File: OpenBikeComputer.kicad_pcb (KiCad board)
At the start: 4 copper layers, 80 x 80 mm, 46 parts, among them J1 USB_C_Receptacle_USB2.0_14P, J2 RJ45_Shielded, J3 RJ45_Shielded, J4 Micro_SD_Card_Det1, J5 Conn_01x24_Socket, J6 Conn_01x03_Pin, U1 nRF54L15-QFXX, U2 nPM1300-QEXX, U3 BQ298012RUGR, U4 BH-18650-A1BJ021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

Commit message: improve design a lot
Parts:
- removed J3: RJ45_Shielded, Connector_RJ:RJ45_Amphenol_54602-x08_Horizontal
- removed REF**: Wuerth_36103205_20x20mm, RF_Shielding:Wuerth_36103205_20x20mm
- removed REF** (x2): 18650, Library:18650
- removed TH1: Thermistor_NTC, Resistor_SMD:R_2512_6332Metric_Pad1.40x3.35mm_HandSolder
- removed U4: BH-18650-A1BJ021, Library:BAT-TH_L77.0-W39.9_BH-18650-A1BJ021
- added C19: 1.5pF, Capacitor_SMD:C_0201_0603Metric, F.Cu at (204.2, 113.4)
- added C20: 2.0pF, Capacitor_SMD:C_0201_0603Metric, F.Cu at (206.2, 113.1)
- added C21: 0.3pF, Capacitor_SMD:C_0201_0603Metric, F.Cu at (207.3, 115.4)
- added J7: RFShield_TwoPieces, RF_Shielding:Laird_Technologies_BMI-S-103_26.21x26.21mm, F.Cu at (197.5, 112.6)
- added J8: Conn_01x02_Socket, Connector_JST:JST_PH_S2B-PH-K_1x02_P2.00mm_Horizontal, B.Cu at (223.2, 93.1)
- added L3: 2.7nH, Inductor_SMD:L_0201_0603Metric, F.Cu at (204.2, 114.1)
- added L4: 3.5nH, Inductor_SMD:L_0201_0603Metric, F.Cu at (205.9, 114.1)
- added L5: 3.5nH, Inductor_SMD:L_0201_0603Metric, F.Cu at (206.2, 115.1)
- J2: footprint Connector_RJ:RJ45_Amphenol_54602-x08_Horizontal -> Connector_RJ:RJ45_Amphenol_RJHSE538X; moved to B.Cu
- moved U7 75.0 mm to (223.1, 152.5)
- moved U6 75.0 mm to (227.4, 152.3)
- moved C1 60.8 mm to (160.3, 112.9)
- moved C2 60.8 mm to (160.3, 114.9)
- moved C4 60.8 mm to (160.3, 118.8)
- moved R2 60.8 mm to (168.9, 114.9)
- moved R1 60.8 mm to (168.9, 112.9)
- moved C10 60.8 mm to (163.2, 120.8)
- moved C11 60.8 mm to (166.1, 112.9)
- moved C12 60.8 mm to (166.1, 114.9)
- moved C13 60.8 mm to (166.1, 116.8)
- moved C14 60.8 mm to (166.1, 118.8)
- moved C8 60.8 mm to (163.2, 116.8)
- moved C9 60.8 mm to (163.2, 118.8)
- moved U3 29.6 mm to (218.8, 94.8), turned to 180 degrees
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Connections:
- J2 pad 1: unconnected-(J2-Pad1) -> GND
- J2 pad 2: GND -> VDDIO
- J2 pad 3: VDDIO -> DETECT1
- J2 pad 4: SENSE1B -> DETECT2
- J2 pad 6: DETECT1 -> SENSE1B
- J2 pad 7: GND -> SENSE2A
- J2 pad 8: unconnected-(J2-Pad8) -> SENSE2B
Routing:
- net /Battery/NTC: track 32.3 -> 1.31 mm
- net Net-(AE2-A): track 0.00 -> 13.5 mm
- net BATGND: track 0.00 -> 4.22 mm
- net GND: track 4.33 -> 6.79 mm, vias 14 -> 16
- net Net-(C19-Pad1): track 0.00 -> 1.74 mm
- net Net-(C20-Pad1): track 0.00 -> 1.46 mm
- net Net-(U1-ANT): track 0.00 -> 1.09 mm

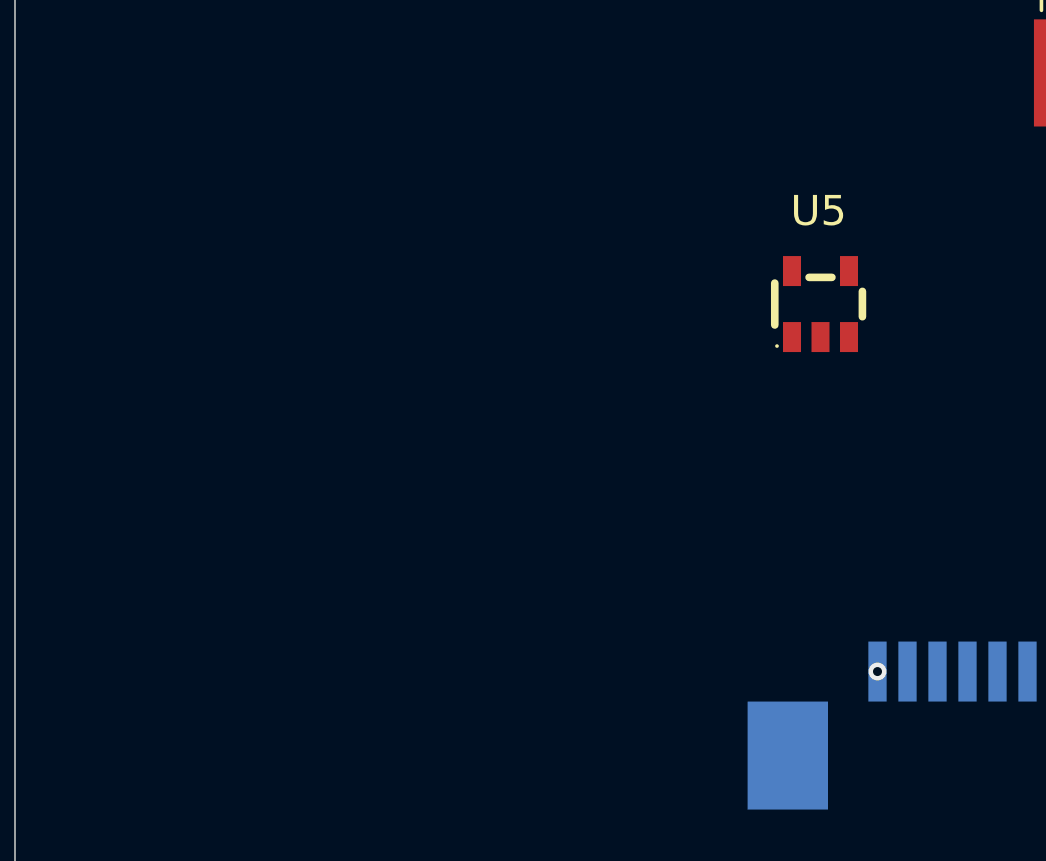
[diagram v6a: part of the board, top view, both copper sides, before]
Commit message: finish oled driver circuit
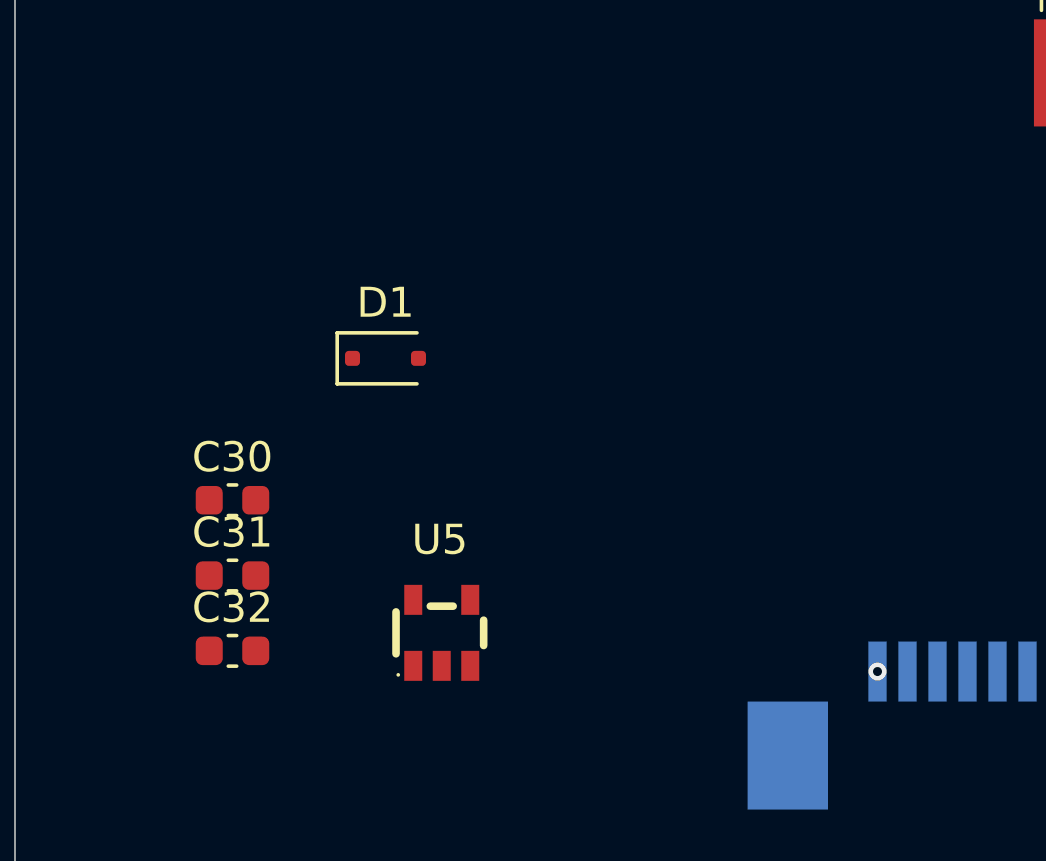
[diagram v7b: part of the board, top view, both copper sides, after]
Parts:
- added C30: 4.7uF, Capacitor_SMD:C_0603_1608Metric, F.Cu at (157.2, 138.5)
- added C31: 120pF, Capacitor_SMD:C_0603_1608Metric, F.Cu at (157.2, 141.1)
- added C32: 4.7uF, Capacitor_SMD:C_0603_1608Metric, F.Cu at (157.2, 143.6)
- added D1: BAT54J, Diode_SMD:D_SOD-323F, F.Cu at (162.3, 133.8)
- moved U5 16.7 mm to (164.2, 143.0)
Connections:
- J5 pad 23: unconnected-(J5-Pin_23-Pad23) -> VOUT
- U1 pad 20: unconnected-(U1-P2.09-Pad20) -> /Display/DISPLAY_SHDN
- U5 pad 1: unconnected-(U5-SW-Pad1) -> Net-(D1-A)
- U5 pad 2: unconnected-(U5-GND-Pad2) -> GND
- U5 pad 3: unconnected-(U5-FB-Pad3) -> Net-(U5-FB)
- U5 pad 4: unconnected-(U5-SHDN#-Pad4) -> /Display/DISPLAY_SHDN
- U5 pad 5: unconnected-(U5-VIN-Pad5) -> /Display/3.0V

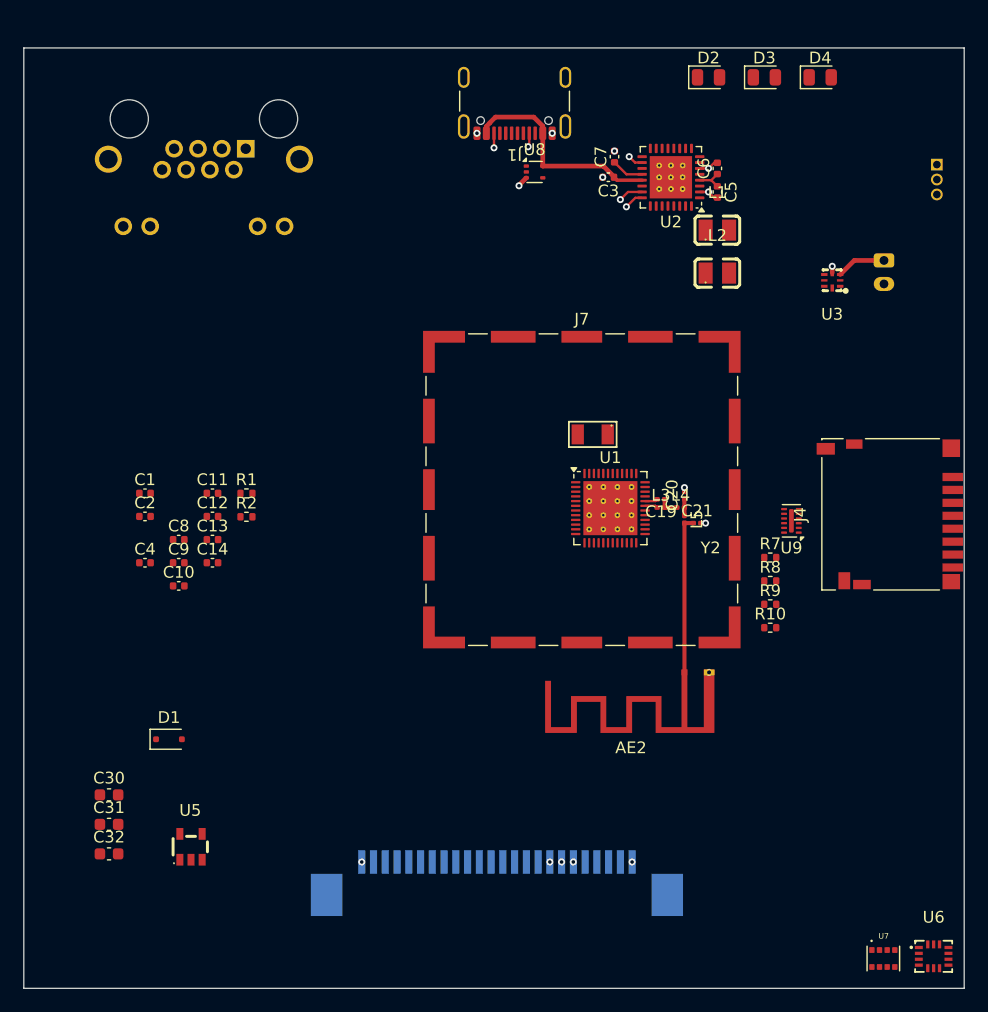
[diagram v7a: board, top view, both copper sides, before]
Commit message: route SD card traces and antenna traces semi-properly
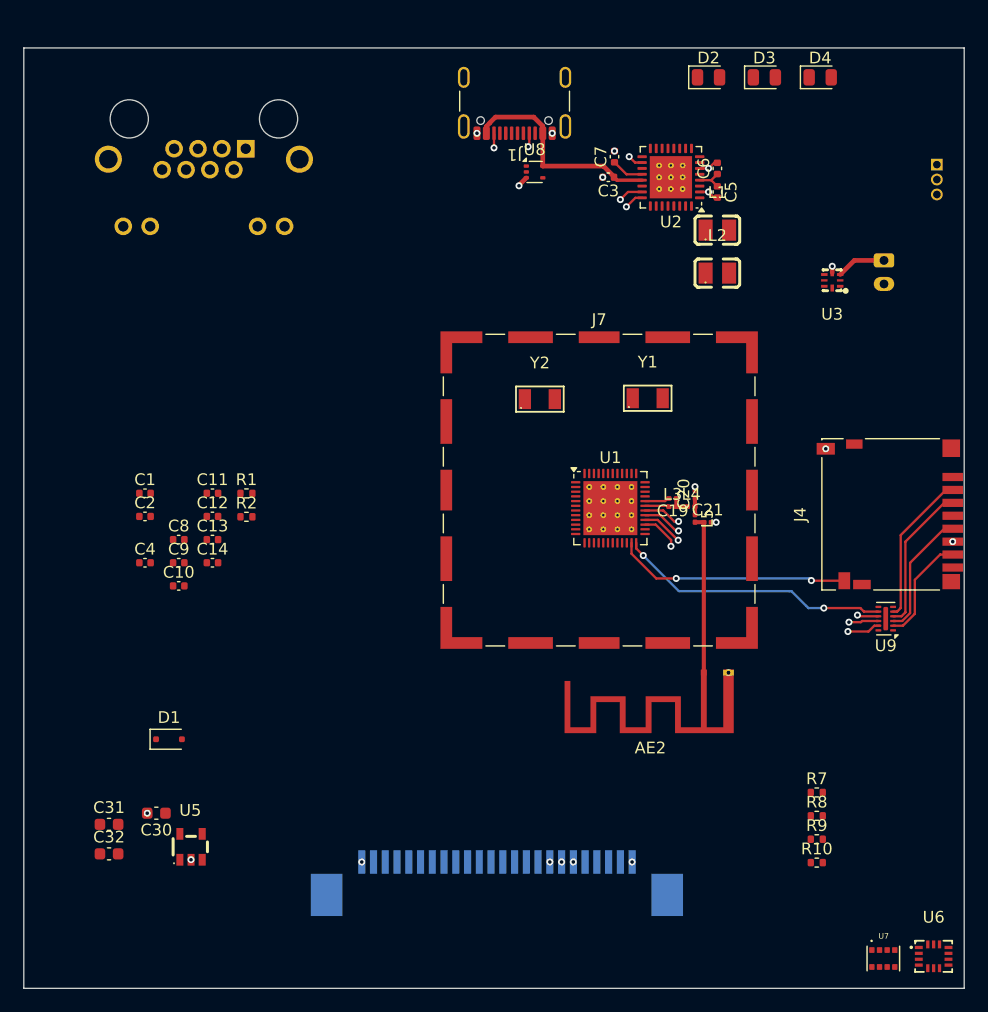
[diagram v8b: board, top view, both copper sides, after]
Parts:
- added Y1: 32MHz, Library:CRYSTAL-SMD_L3.2-W1.5-1, F.Cu at (203.1, 104.8)
- moved R10 20.4 mm to (217.5, 144.3)
- moved R7 20.4 mm to (217.5, 138.3)
- moved R9 20.4 mm to (217.5, 142.3)
- moved R8 20.4 mm to (217.5, 140.3)
- moved U9 11.6 mm to (223.3, 123.5)
- moved Y2 5.41 mm to (193.9, 104.9), turned to 0 degrees
- moved C30 4.32 mm to (161.3, 140.1), turned to 180 degrees
- moved AE2 1.65 mm to (207.8, 128.1)
- moved J7 1.48 mm to (198.9, 112.6)
- moved C19 1.00 mm to (205.2, 113.3)
- moved L3 1.00 mm to (205.2, 114.0)
- moved C20 0.90 mm to (207.1, 113.0)
- moved C21 0.90 mm to (208.2, 115.3)
- moved L4 0.90 mm to (206.8, 114.0)
- moved L5 0.90 mm to (207.1, 115.0)
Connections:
- J4 pad 1: Net-(J4-DAT2) -> unconnected-(J4-DAT2-Pad1)
- J4 pad 8: Net-(J4-DAT1) -> unconnected-(J4-DAT1-Pad8)
- U9 pad 1: Net-(J4-DAT1) -> unconnected-(U9-Ch1_In-Pad1)
- U9 pad 6: Net-(J4-DAT2) -> unconnected-(U9-Ch6_In-Pad6)
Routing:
- net SD_MISO: track 0.00 -> 24.3 mm, vias 0 -> 2
- net SD_SCLK: track 0.00 -> 23.5 mm, vias 0 -> 2
- net SD_MOSI: track 0.00 -> 23.4 mm, vias 0 -> 2
- net SD_CS: track 0.00 -> 23.3 mm, vias 0 -> 2
- net SD_DETECT: track 0.00 -> 20.0 mm, vias 0 -> 2
- net Net-(J4-DAT3/CD): track 0.00 -> 13.0 mm
- net Net-(J4-CMD): track 0.00 -> 12.6 mm
- net Net-(J4-CLK): track 0.00 -> 10.8 mm
- net Net-(J4-DAT0): track 0.00 -> 9.27 mm
- net unconnected-(U1-~{RESET}-Pad30): track 0.00 -> 3.24 mm, vias 0 -> 1
- net Net-(U1-ANT): track 1.09 -> 2.16 mm
- net GND: track 6.79 -> 7.81 mm, vias 16 -> 20
